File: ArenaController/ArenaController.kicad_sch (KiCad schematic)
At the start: 28 parts, among them J1 RJ45, J2 RJ45, J4 RJ45, J5 RJ45, J6 RJ45, J9 Barrel_Jack_MountingPin, Q1 FS3400, Q2 FS3400, Q3 FS3400, Q4 FS3400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

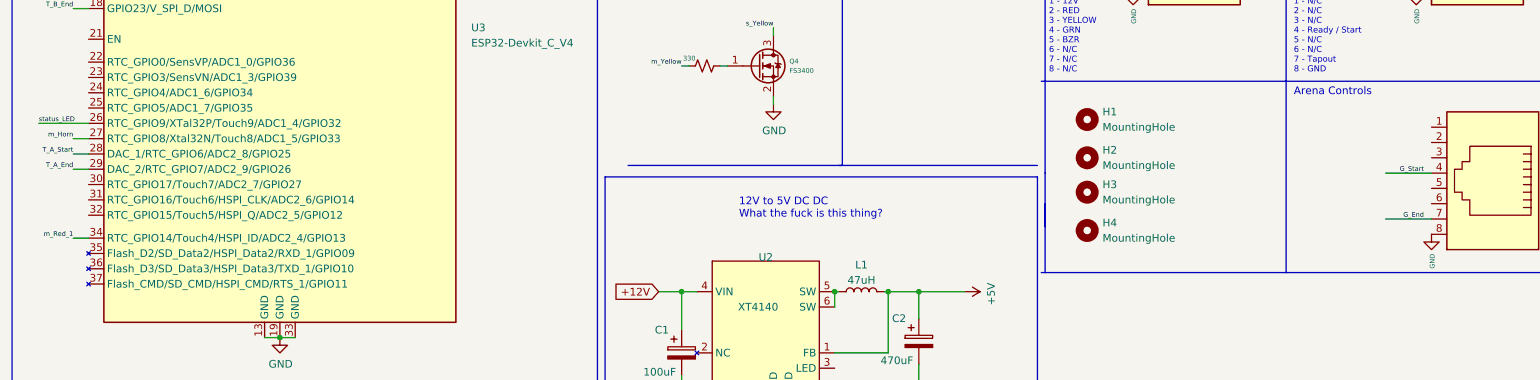
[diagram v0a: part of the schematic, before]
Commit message: Added reset pins back in and broke out the pins in the team control area; should be easier now.  Yay!
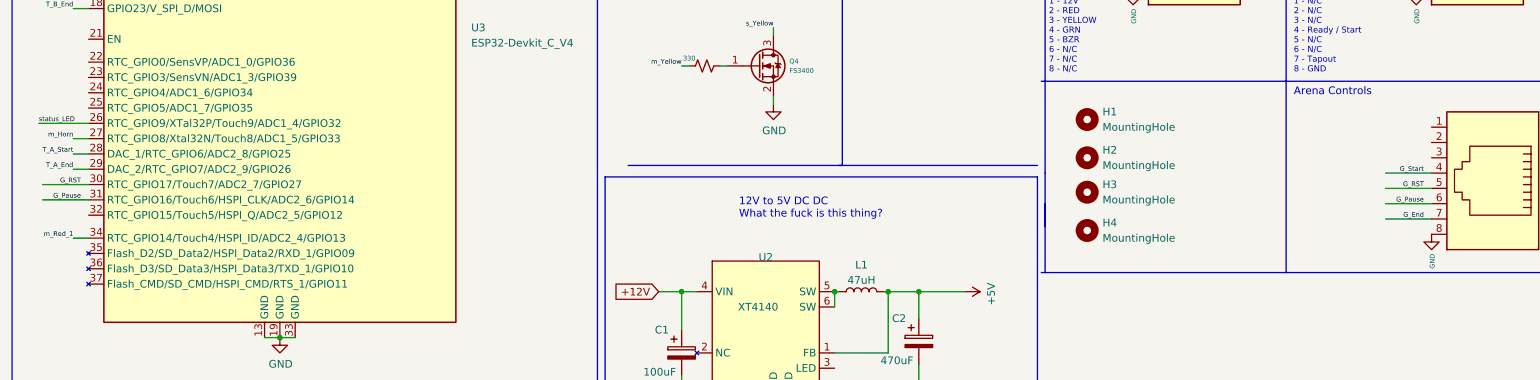
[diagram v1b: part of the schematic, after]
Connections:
- net G_RST: now reaches U3.30 (RTC_GPIO17/Touch7/ADC2_7/GPIO27)
- net G_RST: now also J4.5
- net G_Pause: now reaches U3.31 (RTC_GPIO16/Touch6/HSPI_CLK/ADC2_6/GPIO14)
- net G_Pause: now also J4.6
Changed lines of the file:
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@@
+    (stroke (width 0) (type default))
+  )
+  (wire (pts (xy 243.84 106.68) (xy 251.46 106.68))
     (stroke (width 0) (type default))
   )
@@
     (stroke (width 0) (type default))
   )
+  (wire (pts (xy 20.955 106.045) (xy 28.575 106.045))
+    (stroke (width 0) (type default))
+  )
   (wire (pts (xy 160.655 123.825) (xy 161.29 123.825))
     (stroke (width 0) (type default))
@@
     (stroke (width 0) (type default))
   )
+  (wire (pts (xy 20.955 108.585) (xy 28.575 108.585))
+    (stroke (width 0) (type default))
+  )
   (wire (pts (xy 57.785 131.445) (xy 60.325 131.445))
     (stroke (width 0) (type default))
@@
   )
   (wire (pts (xy 28.575 114.935) (xy 26.035 114.935))
+    (stroke (width 0) (type default))
+  )
+  (wire (pts (xy 243.84 109.22) (xy 251.46 109.22))
     (stroke (width 0) (type default))
   )
@@
     (effects (font (size 0.7874 0.7874)) (justify right bottom))
   )
+  (label "G_Pause" (at 27.305 108.585 180) (fields_autoplaced)
+    (effects (font (size 0.7874 0.7874)) (justify right bottom))
+  )
   (label "m_Green" (at 128.27 57.15 180) (fields_autoplaced)
     (effects (font (size 0.7874 0.7874)) (justify right bottom))
@@
     (effects (font (size 0.7874 0.7874)) (justify right bottom))
   )
+  (label "G_RST" (at 27.305 106.045 180) (fields_autoplaced)
+    (effects (font (size 0.7874 0.7874)) (justify right bottom))
+  )
+  (label "G_Pause" (at 250.19 109.22 180) (fields_autoplaced)
+    (effects (font (size 0.7874 0.7874)) (justify right bottom))
+  )
   (label "m_Red_1" (at 26.035 114.935 180) (fields_autoplaced)
     (effects (font (size 0.7874 0.7874)) (justify right bottom))
@@
     (effects (font (size 0.7874 0.7874)) (justify right bottom))
   )
+  (label "G_RST" (at 250.19 106.68 180) (fields_autoplaced)
+    (effects (font (size 0.7874 0.7874)) (justify right bottom))
+  )

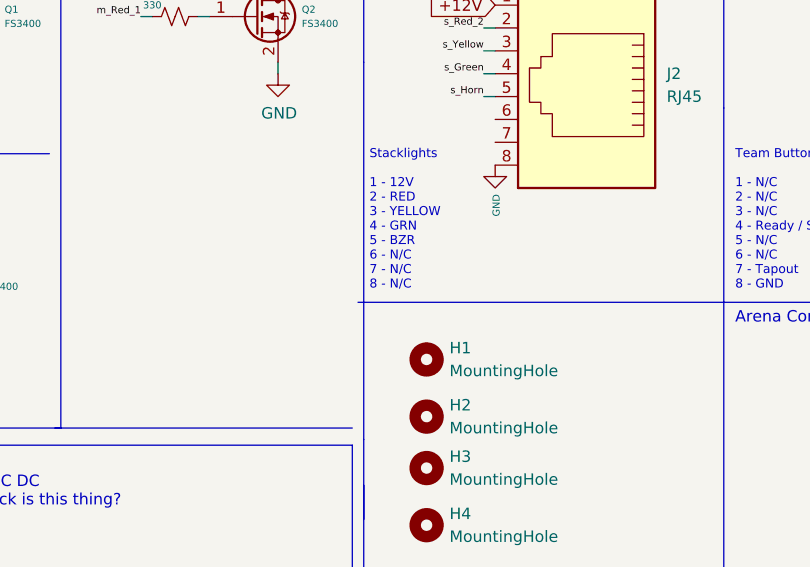
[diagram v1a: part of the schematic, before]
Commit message: Updated PCB revisions, swapped to larger footprint for stacklight connector, release cutting soon.
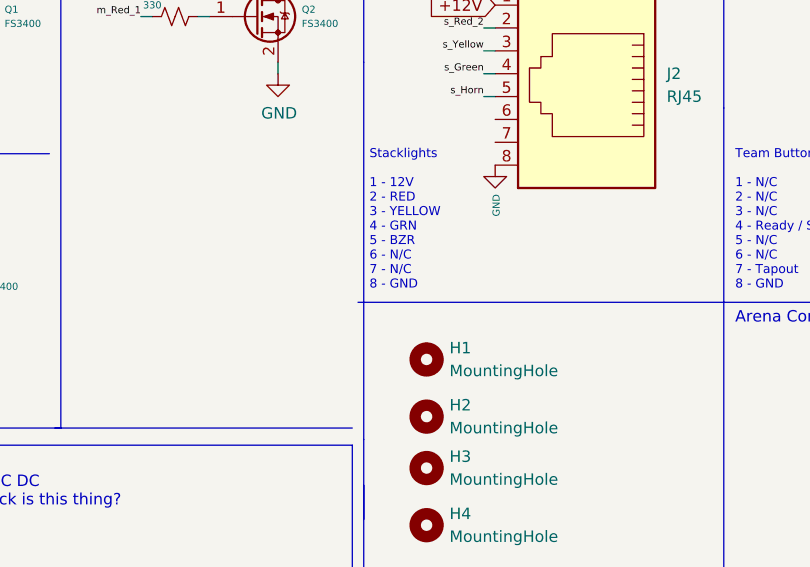
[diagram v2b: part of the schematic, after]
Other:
- note added: "Stacklights 1 - 12V 2 - RED 3 - YELLOW 4 - GRN 5 - BZR 6 - N/C 7 - N/C 8 - GND"
- note removed: "Stacklights 1 - 12V 2 - RED 3 - YELLOW 4 - GRN 5 - BZR 6 - N/C 7 - N/C 8 - N/C"
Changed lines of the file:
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@@
     (effects (font (size 1.27 1.27)) (justify left bottom))
   )
-  (text "Stacklights\n\n1 - 12V\n2 - RED\n3 - YELLOW\n4 - GRN\n5 - BZR\n6 - N/C\n7 - N/C\n8 - N/C"
+  (text "Stacklights\n\n1 - 12V\n2 - RED\n3 - YELLOW\n4 - GRN\n5 - BZR\n6 - N/C\n7 - N/C\n8 - GND"
     (at 187.96 87.63 0)
     (effects (font (size 1 1)) (justify left bottom))

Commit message: chip thing etc
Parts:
- L1: footprint Inductor_SMD:L_0603_1608Metric -> Inductor_SMD:L_1210_3225Metric_Pad1.42x2.65mm_HandSolder; LCSC https://www.lcsc.com/product-detail/Inductors-SMD_PROD-Tech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 -> https://www.lcsc.com/product-detail/Inductors-SMD_TDK-NLV32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
- R1, R2, R3, R4, R5: footprint Resistor_SMD:R_0603_1608Metric_Pad0.98x0.95mm_HandSolder -> Resistor_SMD:R_1206_3216Metric_Pad1.30x1.75mm_HandSolder; LCSC https://www.lcsc.com/product-detail/Chip-Resistor-Surface-Mount_Walsin-Tech-Corp-WR06X331JTL_C384242.html -> https://www.lcsc.com/product-detail/Chip-Resistor-Surface-Mount_UNI-ROYAL-Uniroyal-Elec-1206W4J0331T5E_C25374.html
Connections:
- net m_Red_1: now also R5.2; no longer R4.2
- net m_Red_2: now also R4.2; no longer R3.2
- net m_Yellow: now also R3.2; no longer R5.2
- net at Q2.1 (G): now also R5.1; no longer R4.1
- net at Q4.1 (G): now also R3.1; no longer R5.1
- net at Q5.1 (G): now also R4.1; no longer R3.1

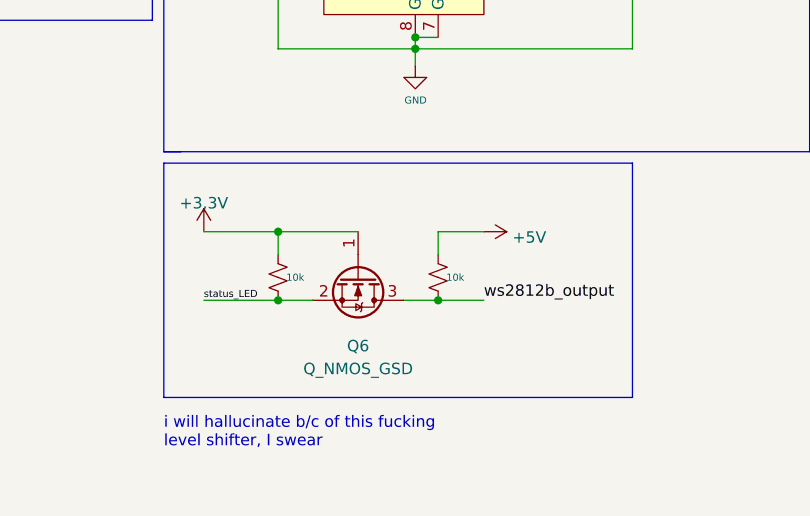
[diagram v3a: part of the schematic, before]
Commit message: Added Littelfuse TVS to the schematic.
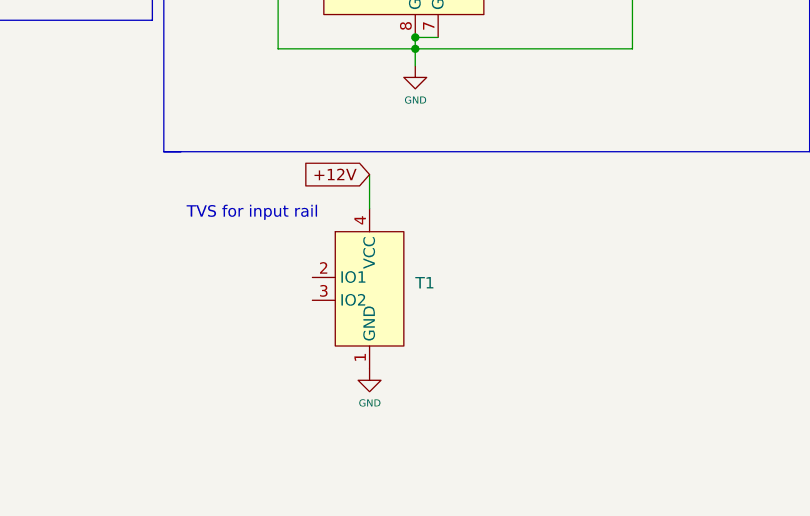
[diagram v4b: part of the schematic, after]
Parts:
- removed Q6: Q_NMOS_GSD, Package_TO_SOT_SMD:SOT-23, symbol Device:Q_NMOS_GSD
- removed R16, R7: 10k, Resistor_SMD:R_0603_1608Metric_Pad0.98x0.95mm_HandSolder, symbol Device:R_Small_US
- added T1: ~, Package_TO_SOT_SMD:SOT-143_Handsoldering, symbol symbols:SR70-02CTG
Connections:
- net +12V: now also T1.4 (VCC)
- net GND: now also T1.1 (GND)
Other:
- note added: "TVS for input rail"
- note removed: "i will hallucinate b/c of this fucking level shifter, I swear"

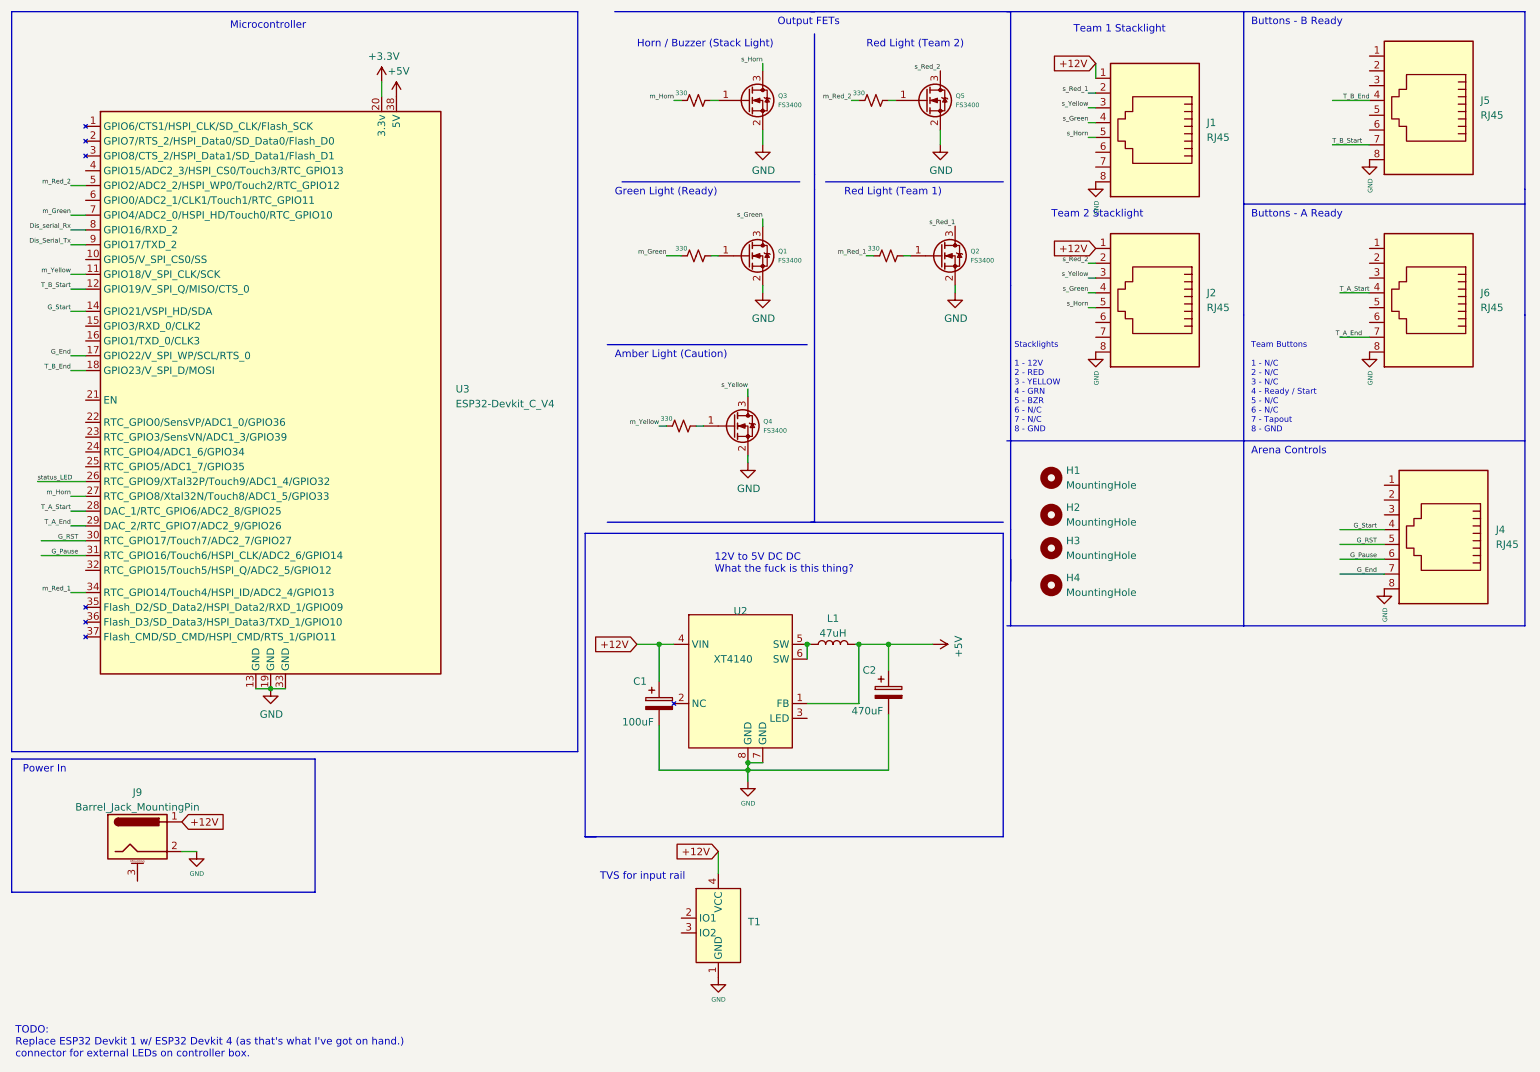
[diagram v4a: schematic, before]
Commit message: Update board to have less skullfscked routing and removed unused projects.
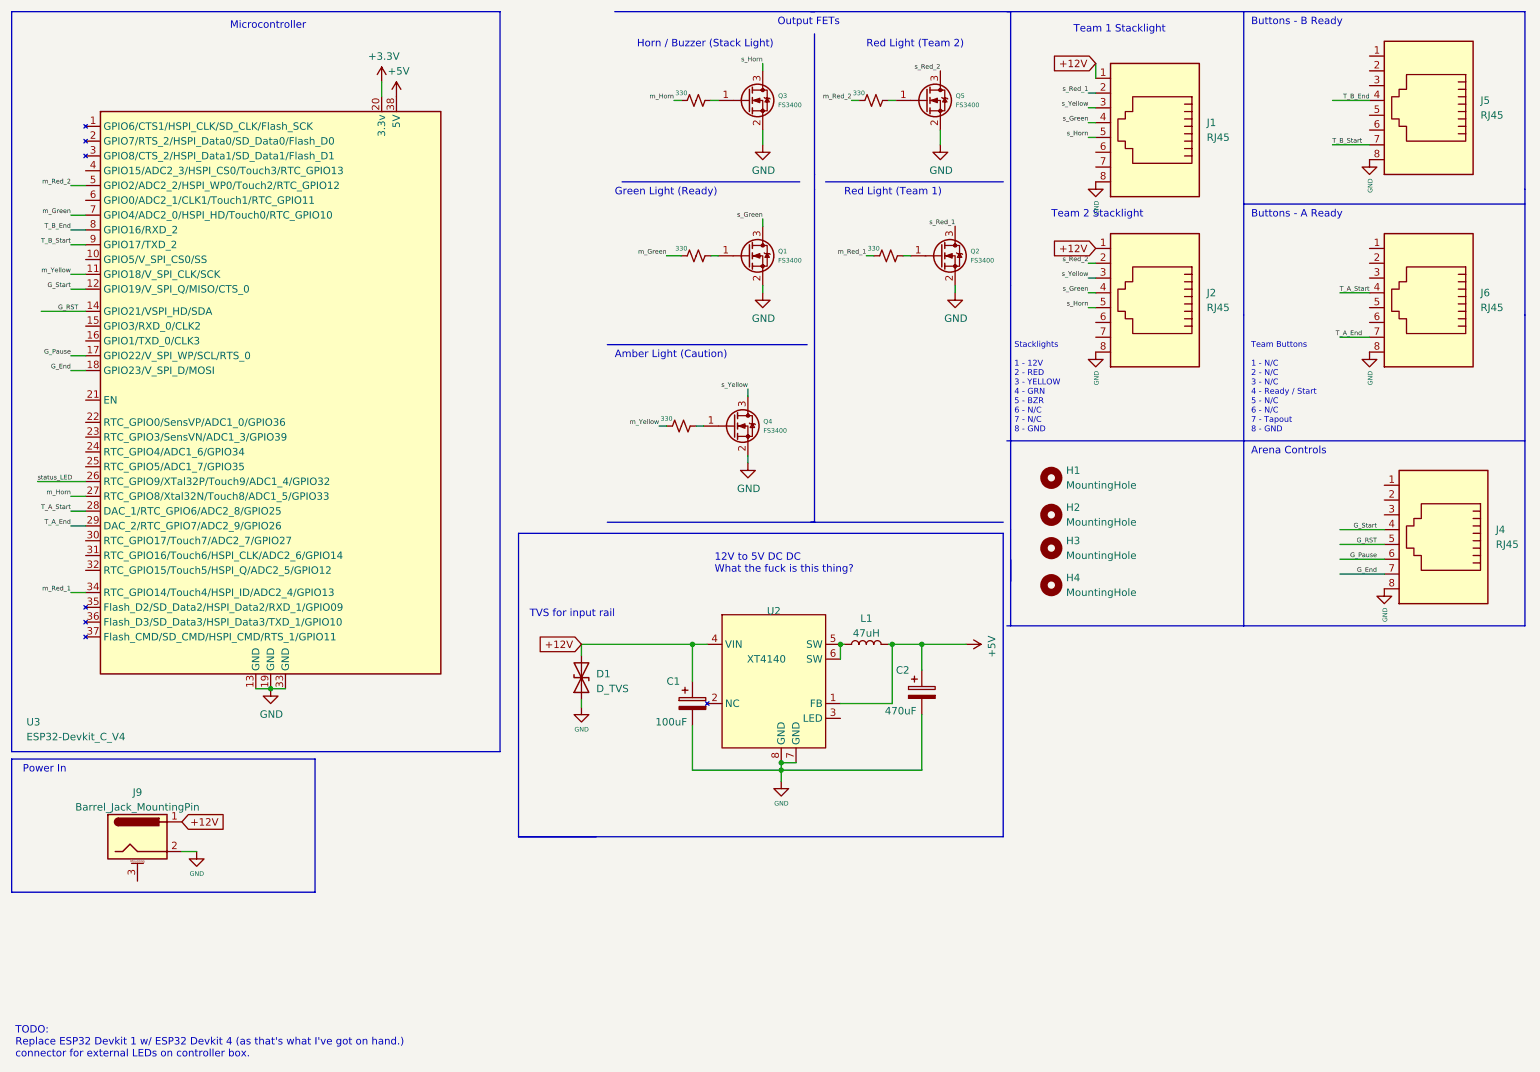
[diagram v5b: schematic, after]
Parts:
- removed T1: ~, Package_TO_SOT_SMD:SOT-143_Handsoldering, symbol symbols:SR70-02CTG
- added D1: D_TVS, Diode_SMD:D_SOD-123F, symbol Device:D_TVS
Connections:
- net Dis_Serial_Tx is gone; now on net T_B_Start: U3.9 (GPIO17/TXD_2)
- net Dis_serial_Rx is gone; now on net T_B_End: U3.8 (GPIO16/RXD_2)
- net +12V: now also D1.2 (A2)
- net GND: now also D1.1 (A1)
- net G_End: now also U3.18 (GPIO23/V_SPI_D/MOSI); no longer U3.17 (GPIO22/V_SPI_WP/SCL/RTS_0)
- net G_Pause: now also U3.17 (GPIO22/V_SPI_WP/SCL/RTS_0); no longer U3.31 (RTC_GPIO16/Touch6/HSPI_CLK/ADC2_6/GPIO14)
- net G_RST: now also U3.14 (GPIO21/VSPI_HD/SDA); no longer U3.30 (RTC_GPIO17/Touch7/ADC2_7/GPIO27)
- net G_Start: now also U3.12 (GPIO19/V_SPI_Q/MISO/CTS_0); no longer U3.14 (GPIO21/VSPI_HD/SDA)
- net T_B_End: no longer U3.18 (GPIO23/V_SPI_D/MOSI)
- net T_B_Start: no longer U3.12 (GPIO19/V_SPI_Q/MISO/CTS_0)
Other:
- moved on the sheet: C1, C2, L1, U2
